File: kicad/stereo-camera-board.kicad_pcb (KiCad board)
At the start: 4 copper layers, 57 x 70 mm, 82 parts, among them IC1 ZLDO1117G33TA, IC2 MCP1700T-2502E/TT, IC3 SN74LVC1T45DCKR, IC4 SN74LVC1T45DCKR, IC5 SN74LVC1T45DCKR, T1 2n2222a, T2 2N2907A, U1 GSB311231HR, U2 ATXMEGA256A3-AU, U3 MAX3207E

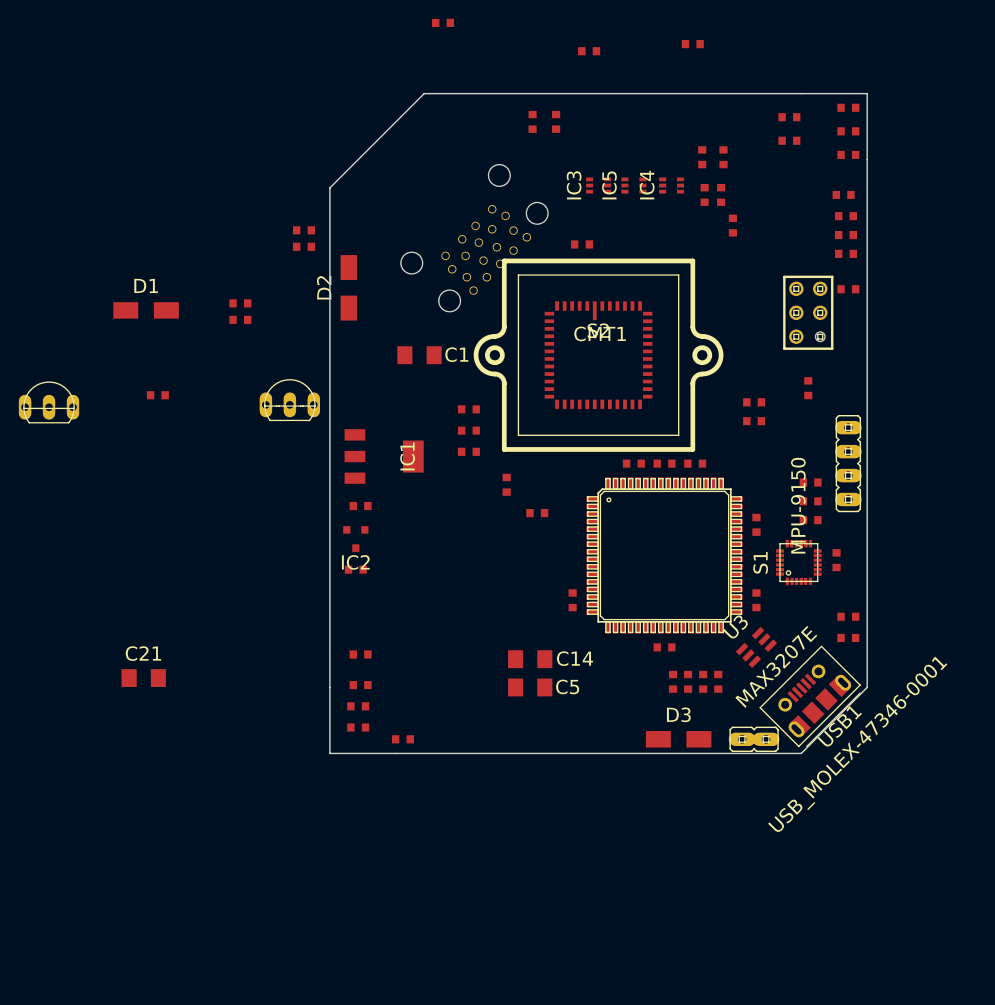
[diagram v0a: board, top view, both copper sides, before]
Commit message: Added mpu-9250 mod file Modified pcb layout
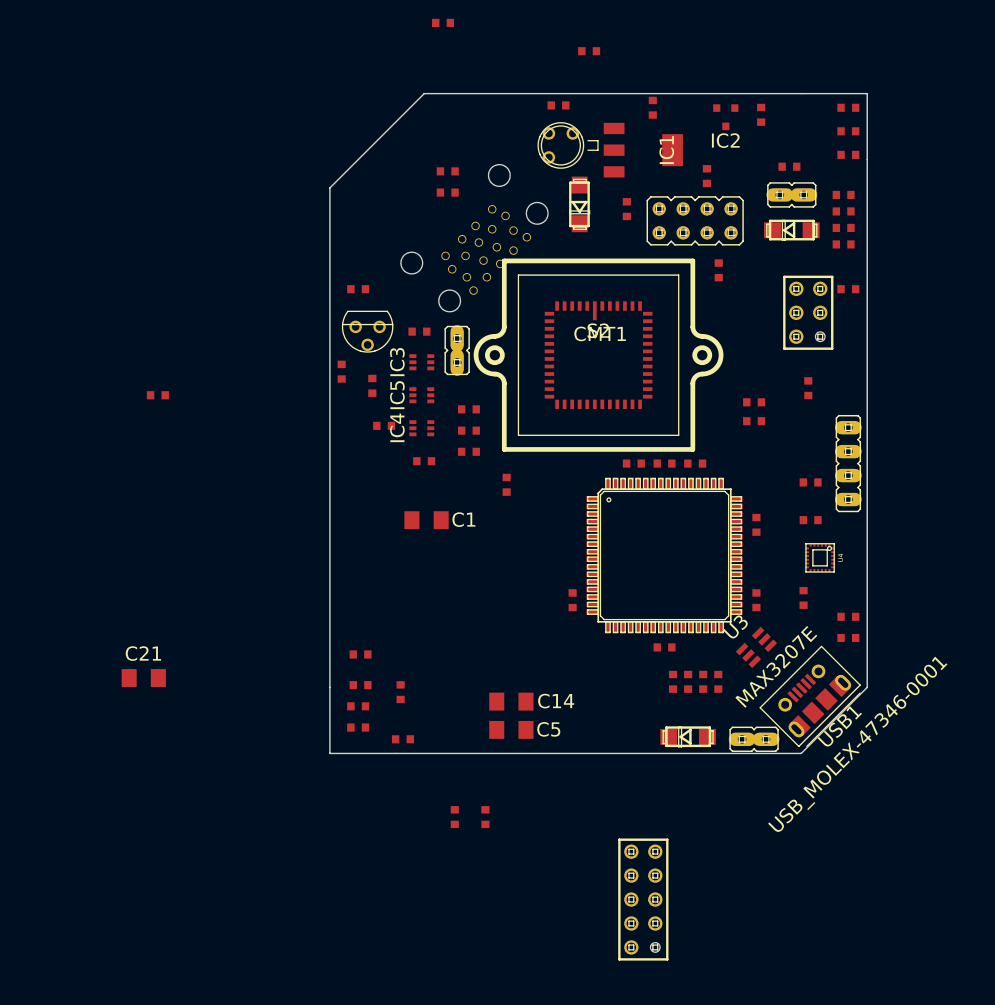
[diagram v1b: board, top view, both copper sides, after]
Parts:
- removed C29: 10nf, SMD-0603
- removed S1: MPU-9150, mpu-9150
- added J1: ~, jumper-JP1, F.Cu at (169.0, 90.8)
- added JP1: ~, jumper-JP4Q, F.Cu at (158.8, 93.5)
- added JP2: JP_JP1Q, jumper-JP1, F.Cu at (133.5, 107.2)
- added JP3: AVR-JTAG-10, atmel-AVR-JTAG-10, F.Cu at (153.2, 165.5)
- added U4: MPU-9250, MPU-9250, F.Cu at (172.0, 129.2)
- C26: value 2.2nf -> .1uf
- C27: value .1uf -> 10nf
- D1, D2, D3: footprint do-214ac -> diode-DO214AC
- T1: footprint transistor-TO92-EBC -> transistor-TO92
- T2: footprint transistor-TO92-EBC -> transistor-TO18
- moved R21 75.6 mm to (133.2, 156.8)
- moved R22 73.7 mm to (136.5, 156.8)
- moved D1 69.0 mm to (169.0, 94.5)
- moved C24 61.8 mm to (127.5, 143.5)
- moved IC2 59.5 mm to (162.0, 82.5)
- moved C7 59.4 mm to (165.8, 82.2), turned to 270 degrees
- moved C6 58.3 mm to (154.2, 81.5), turned to 270 degrees
- moved IC1 42.6 mm to (153.2, 86.0)
- moved C22 42.3 mm to (130.0, 119.0), turned to 180 degrees
- moved T2 38.9 mm to (144.5, 85.5), turned to 180 degrees
- moved IC4 37.0 mm to (129.8, 115.5)
- moved T1 34.6 mm to (124.0, 104.8), turned to 180 degrees
- moved IC5 31.6 mm to (129.8, 112.0)
- moved R20 30.9 mm to (144.2, 81.2)
- moved IC3 26.5 mm to (129.8, 108.5)
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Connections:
- C10 pad 2: N-0000025 (its old number) -> N-00000115
- C12 pad 2: N-0000025 (its old number) -> N-00000115
- C16 pad 1: N-0000013 (its old number) -> N-00000106
- C17 pad 1: N-0000013 (its old number) -> N-00000106
- C18 pad 1: N-0000013 (its old number) -> N-00000106
- C19 pad 1: N-0000013 (its old number) -> N-00000106
- C2 pad 2: N-0000025 (its old number) -> N-00000115
- C20 pad 1: N-0000013 (its old number) -> N-00000106
- C23 pad 1: N-00000143 -> N-00000107
- C26 pad 1: N-0000060 (its old number) -> N-0000037
- C26 pad 2: N-00000101 (its old number) -> N-0000038
- C27 pad 1: N-0000071 -> N-0000037
- C27 pad 2: N-00000101 (its old number) -> N-0000038
- C28 pad 1: N-00000101 (its old number) -> N-00000143
- C3 pad 2: N-0000025 (its old number) -> N-00000115
- C4 pad 2: N-0000025 (its old number) -> N-00000115
- C8 pad 1: N-0000026 -> N-0000028
- C8 pad 2: N-0000023 -> N-000003
- C9 pad 2: N-0000025 (its old number) -> N-00000115
- EXT_SENSOR1 pad 1: N-0000071 -> N-00000114
- EXT_SENSOR1 pad 2: N-00000101 (its old number) -> N-00000108
- FB2 pad 1: N-00000143 -> N-00000106
- FB2 pad 2: N-0000013 (its old number) -> N-00000107
- IC1 pad 3: N-0000039 -> N-0000081
- IC3 pad 5: N-0000034 (its old number) -> N-0000050
- IC4 pad 3: N-0000016 -> N-00000122
- IC4 pad 5: N-0000029 (its old number) -> N-0000042
- IC5 pad 3: N-0000037 -> N-0000051
- IC5 pad 5: N-0000030 (its old number) -> N-0000041
- JP6 pad 2: N-00000122 -> N-00000132
- R10 pad 1: N-0000035 (its old number) -> N-0000073
- R10 pad 2: N-0000088 (its old number) -> N-0000053
- R15 pad 1: N-0000031 -> N-0000052
- R17 pad 1: N-0000041 -> N-0000072
- R17 pad 2: N-0000035 (its old number) -> N-0000073
- R18 pad 1: N-0000040 -> N-0000071
- R18 pad 2: N-00000147 -> N-00000139
- R19 pad 2: N-00000127 (its old number) -> N-00000138
- R20 pad 1: N-0000039 -> N-0000081
- R20 pad 2: N-00000147 -> N-00000139
- R21 pad 1: N-00000146 -> N-00000138
- R23 pad 2: N-0000036 (its old number) -> N-0000080
- R5 pad 1: N-0000025 (its old number) -> N-00000115
- R5 pad 2: N-0000058 (its old number) -> N-0000067
- R7 pad 1: N-00000127 (its old number) -> N-0000061
- S2 pad 12: N-0000025 (its old number) -> N-00000115
- S2 pad 13: N-0000025 (its old number) -> N-00000115
- S2 pad 16: N-00000111 -> N-0000066
- S2 pad 17: N-00000112 -> N-0000065
- S2 pad 18: N-00000113 (its old number) -> N-000008
- S2 pad 19: N-00000114 -> N-0000032
- S2 pad 20: N-000002 (its old number) -> N-0000033
- S2 pad 21: N-00000109 (its old number) -> N-0000023
- S2 pad 22: N-0000064 (its old number) -> N-0000011
- S2 pad 23: N-0000099 (its old number) -> N-0000016
- S2 pad 26: N-00000105 (its old number) -> N-00000118
- S2 pad 27: N-0000027 (its old number) -> N-00000120
- S2 pad 28: N-000003 -> N-00000119
- S2 pad 29: N-0000025 (its old number) -> N-00000115
- S2 pad 30: N-0000011 -> N-00000115
- S2 pad 31: N-000006 (its old number) -> N-00000115
- S2 pad 32: N-0000058 (its old number) -> N-0000067
- S2 pad 33: N-0000063 (its old number) -> N-00000117
- S2 pad 34: N-0000025 (its old number) -> N-00000115
- S2 pad 38: N-0000025 (its old number) -> N-00000115
- S2 pad 41: N-00000115 -> N-00000111
- S2 pad 42: N-0000098 (its old number) -> N-00000112
- S2 pad 43: N-0000078 (its old number) -> N-000005
- S2 pad 44: N-0000079 (its old number) -> N-000009
- S2 pad 45: N-0000080 -> N-00000121
- S2 pad 46: N-00000107 -> N-00000123
- S2 pad 48: N-0000025 (its old number) -> N-00000115
- S2 pad 7: N-0000025 (its old number) -> N-00000115
- U1 pad 10: N-0000054 -> N-00000100
- U1 pad 12: N-00000127 (its old number) -> N-00000138
- U1 pad 3: N-00000127 (its old number) -> N-0000061
- U2 pad 1: N-0000098 (its old number) -> N-00000138
- U2 pad 12: N-00000127 (its old number) -> N-0000054
- U2 pad 15: N-0000013 (its old number) -> N-00000106
- U2 pad 18: N-0000063 (its old number) -> N-0000016
- U2 pad 19: N-0000058 (its old number) -> N-0000011
- U2 pad 2: N-00000115 -> N-0000053
- U2 pad 20: N-000003 -> N-0000023
- U2 pad 21: N-0000027 (its old number) -> N-0000033
- U2 pad 22: N-00000105 (its old number) -> N-0000032
- U2 pad 23: N-0000047 -> N-000008
- U2 pad 25: N-0000013 (its old number) -> N-00000106
- U2 pad 26: N-0000099 (its old number) -> N-0000065
- U2 pad 27: N-0000064 (its old number) -> N-0000066
- U2 pad 28: N-000002 (its old number) -> N-00000110
- U2 pad 3: N-00000114 -> N-00000140
- U2 pad 35: N-0000013 (its old number) -> N-00000106
- U2 pad 36: N-0000014 (its old number) -> N-00000122
- U2 pad 37: N-00000100 -> N-0000080
- U2 pad 39: N-0000088 (its old number) -> N-00000128
- U2 pad 4: N-00000113 (its old number) -> N-00000141
- U2 pad 40: N-0000011 -> N-0000039
- U2 pad 41: N-0000036 (its old number) -> N-0000040
- U2 pad 42: N-0000037 -> N-00000125
- U2 pad 43: N-0000016 -> N-00000124
- U2 pad 45: N-0000013 (its old number) -> N-00000106
- U2 pad 46: N-00000121 -> N-0000067
- U2 pad 47: N-0000051 -> N-00000117
- U2 pad 48: N-0000052 -> N-00000111
- U2 pad 49: N-0000053 -> N-00000112
- U2 pad 5: N-00000112 -> N-00000142
- U2 pad 50: N-000006 (its old number) -> N-000005
- U2 pad 51: N-0000034 (its old number) -> N-000009
- U2 pad 53: N-0000013 (its old number) -> N-00000106
- U2 pad 54: N-0000029 (its old number) -> N-00000121
- U2 pad 55: N-0000030 (its old number) -> N-00000123
- U2 pad 6: N-00000111 -> N-0000051
- U2 pad 61: N-00000143 -> N-00000107
- U2 pad 62: N-0000080 -> N-00000119
- U2 pad 63: N-0000079 (its old number) -> N-00000120
- U2 pad 64: N-0000078 (its old number) -> N-00000118
- U2 pad 7: N-00000110 -> N-0000041
- U2 pad 8: N-00000107 -> N-0000042
- U2 pad 9: N-00000109 (its old number) -> N-0000050
- USB1 pad 1: N-0000031 -> N-0000052

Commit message: Rotated xmega 45d Repositioned some other small components on pcb Cut bottom right corner to match top left
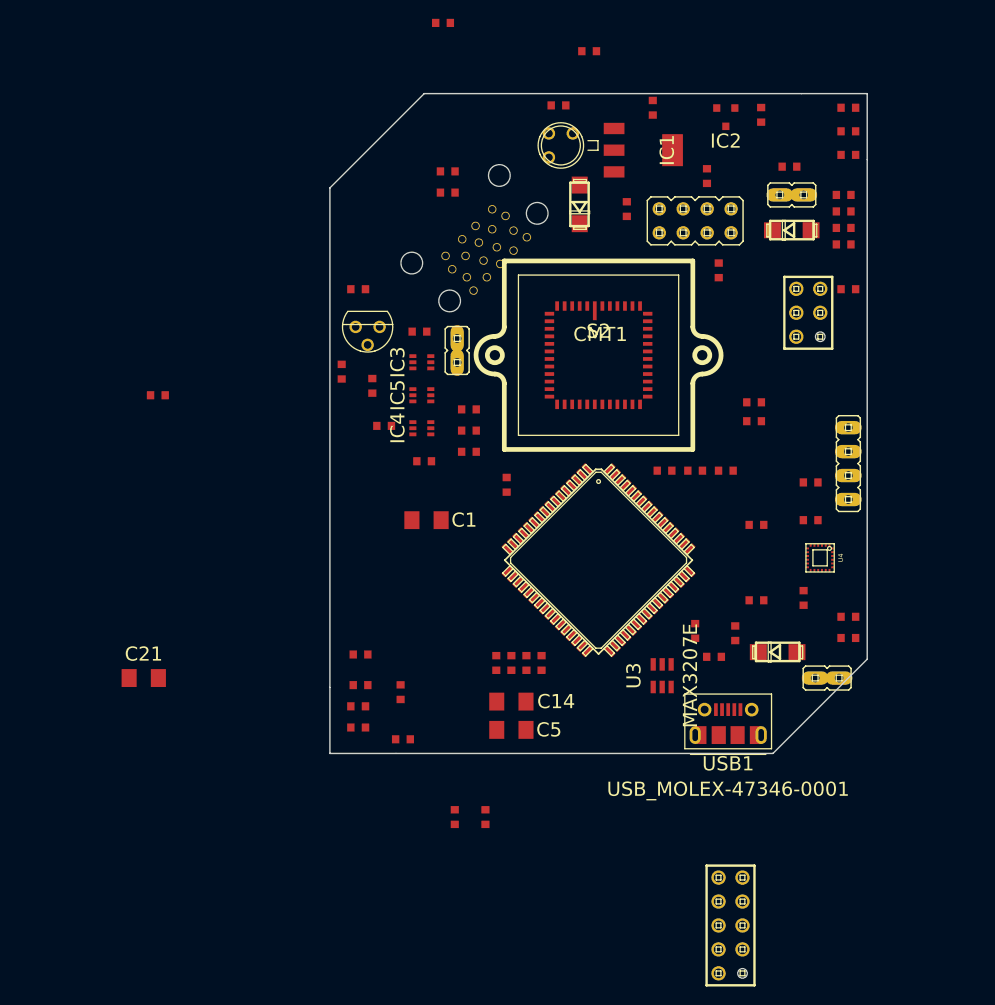
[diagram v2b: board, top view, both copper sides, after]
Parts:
- moved R23 27.1 mm to (163.0, 137.2)
- moved R11 18.9 mm to (139.2, 140.4)
- moved R12 18.9 mm to (137.7, 140.4)
- moved R14 18.9 mm to (140.8, 140.4)
- moved R15 18.9 mm to (142.4, 140.4)
- moved C16 16.2 mm to (160.8, 139.8), turned to 180 degrees
- moved D3 13.1 mm to (167.5, 139.2)
- moved USB1 11.3 mm to (162.2, 149.5), turned to 0 degrees
- moved U3 10.4 mm to (155.2, 141.8), turned to 90 degrees
- moved JP6 10.1 mm to (172.8, 142.0)
- moved JP3 9.65 mm to (162.5, 168.2)
- moved U2 7.02 mm to (148.5, 129.5), turned to 315 degrees
- moved C17 3.69 mm to (158.8, 137.0), turned to 270 degrees
- moved C20 3.34 mm to (162.0, 120.0)
- moved C23 3.34 mm to (155.5, 120.0)
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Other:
- outline, holes or cut-outs redrawn

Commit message: Routed differential signals Routed 9-axis sensor Routed a few small components Set up routing rules for OshPark Fixed netlist Rearranged some nets for better fit
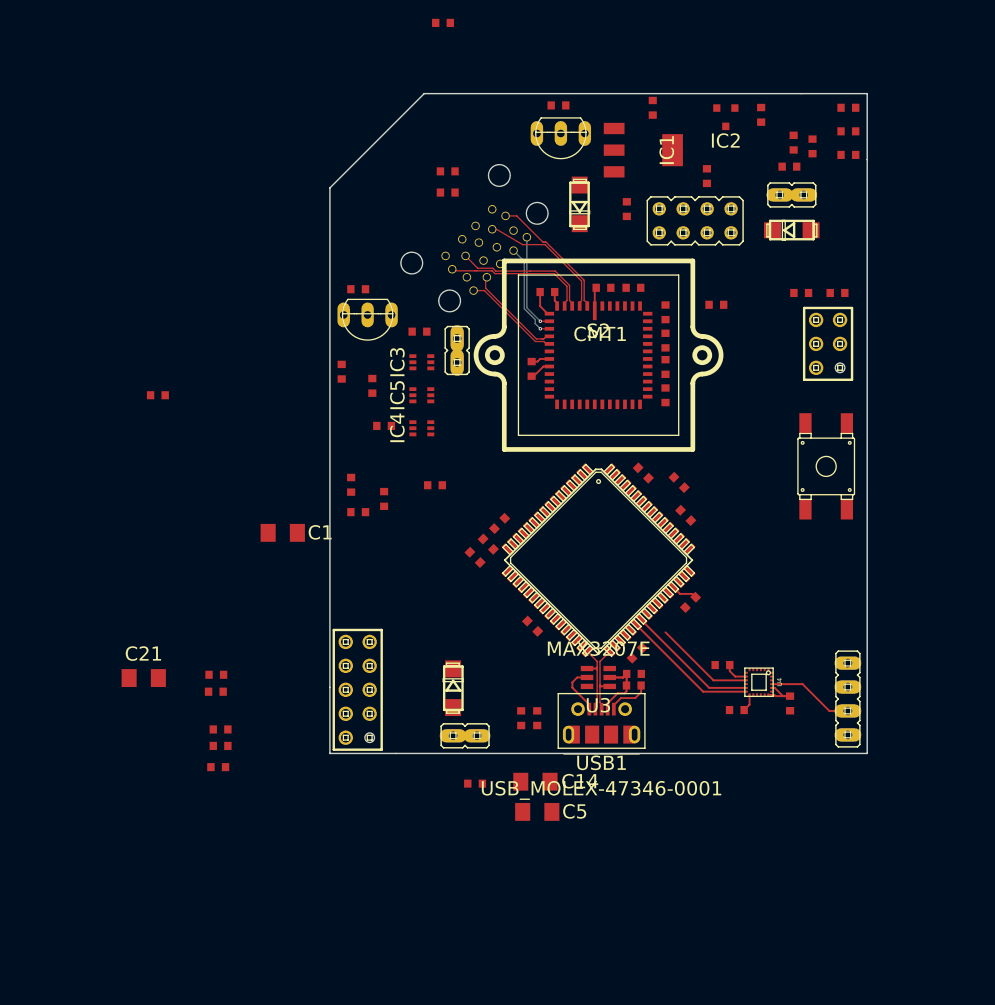
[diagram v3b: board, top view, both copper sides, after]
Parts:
- added P1: FSM4JSMA-SMD, switch-misc-FSM4JSMA-SMD, F.Cu at (172.7, 119.5)
- T1: footprint transistor-TO92 -> transistor-TO92-EBC
- T2: footprint transistor-TO18 -> transistor-TO92-EBC
- moved R12 63.6 mm to (169.2, 85.2)
- moved R11 63.4 mm to (171.2, 85.6)
- moved JP3 46.8 mm to (123.0, 143.2)
- moved JP6 38.9 mm to (134.3, 148.1)
- moved R23 38.2 mm to (152.2, 100.6), turned to 0 degrees
- moved R21 36.9 mm to (122.2, 121.5)
- moved R22 35.4 mm to (125.8, 123.0)
- moved D3 34.6 mm to (133.1, 143.1), turned to 270 degrees
- moved C11 34.1 mm to (170.0, 101.2)
- moved R3 33.9 mm to (135.4, 129.2), turned to 315 degrees
- moved C22 31.6 mm to (108.0, 141.7), turned to 0 degrees
- moved R4 31.1 mm to (136.8, 127.8), turned to 315 degrees
- moved C12 26.3 mm to (155.6, 109.0), turned to 270 degrees
- moved C26 25.4 mm to (163.2, 145.4), turned to 180 degrees
- moved EXT_SENSOR1 25.0 mm to (174.9, 144.2)
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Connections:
- D2 pad A: N-00000126 (its old number) -> N-00000132
- IC1 pad 3: N-0000081 -> N-0000080
- JP1 pad 2: N-000006 (its old number) -> N-0000020
- JP1 pad 4: N-0000012 (its old number) -> N-000003
- JP1 pad 6: N-000002 (its old number) -> N-0000055
- JP1 pad 8: N-0000029 (its old number) -> N-0000056
- JP6 pad 1: N-0000031 (its old number) -> N-0000038
- R10 pad 1: N-0000073 -> N-0000083
- R15 pad 1: N-0000052 -> N-0000038
- R17 pad 1: N-0000072 (its old number) -> N-0000082
- R17 pad 2: N-0000073 -> N-0000083
- R18 pad 1: N-0000071 (its old number) -> N-0000081
- R18 pad 2: N-00000139 (its old number) -> N-00000143
- R20 pad 1: N-0000081 -> N-0000080
- R20 pad 2: N-00000139 (its old number) -> N-00000143
- S2 pad 10: N-0000012 (its old number) -> N-0000055
- S2 pad 11: N-000006 (its old number) -> N-0000056
- S2 pad 8: N-000002 (its old number) -> N-000003
- S2 pad 9: N-0000029 (its old number) -> N-0000020
- U1 pad 14: N-0000012 (its old number) -> N-000003
- U1 pad 15: N-000006 (its old number) -> N-0000020
- U1 pad 17: N-000002 (its old number) -> N-0000055
- U1 pad 18: N-0000029 (its old number) -> N-0000056
- U2 pad 32: N-0000078 (its old number) -> N-0000073
- U2 pad 33: N-0000077 (its old number) -> N-0000074
- U3 pad 1: N-0000078 (its old number) -> N-0000074
- U3 pad 4: N-0000077 (its old number) -> N-0000073
- U3 pad 5: N-0000031 (its old number) -> N-0000038
- USB1 pad 1: N-0000052 -> N-0000038
- USB1 pad 2: N-0000078 (its old number) -> N-0000073
- USB1 pad 3: N-0000077 (its old number) -> N-0000074
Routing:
- net N-00000115: track 0.00 -> 14.6 mm
- net N-00000130: track 0.00 -> 14.6 mm
- net N-0000069: track 0.00 -> 14.2 mm
- net N-00000129: track 0.00 -> 14.1 mm
- net N-0000072: track 0.00 -> 13.8 mm
- net N-0000064: track 0.00 -> 13.6 mm
- net N-0000037: track 0.00 -> 10.7 mm
- net N-000003: track 0.00 -> 10.0 mm, vias 0 -> 1
- net N-0000020: track 0.00 -> 10.0 mm, vias 0 -> 1
- net N-0000056: track 0.00 -> 9.95 mm
- net N-0000055: track 0.00 -> 9.91 mm
- net N-00000111: track 0.00 -> 9.26 mm
- net N-0000073: track 0.00 -> 8.87 mm
- net N-0000074: track 0.00 -> 8.78 mm
- net N-0000077: track 0.00 -> 6.96 mm
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- added copper zone on Inner1.Cu, net (none)
- added copper zone on Inner2.Cu, net (none)
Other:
- outline, holes or cut-outs redrawn
- net class Default: clearance 0.254 -> 0.1; trace_width 0.254 -> 0.2032
- net class USB added: clearance 0.1, trace_width 0.127, via_dia 0.3556, via_drill 0.254
- rule trace_clearance: 0.254 -> 0.1
- rule trace_min: 0.254 -> 0.127
- rule via_min_drill: 0.508 -> 0.254
- rule via_min_size: 0.889 -> 0.1016

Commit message: Minor component placement adjustments
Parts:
- moved C27 1.32 mm to (163.0, 140.7), turned to 90 degrees
- moved C26 0.79 mm to (163.7, 144.8)
- moved C6 0.19 mm to (154.4, 81.6), turned to 0 degrees
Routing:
- net N-00000143: track 0.00 -> 32.1 mm
- net N-0000091: track 0.00 -> 27.5 mm
- net N-0000036: track 0.00 -> 25.8 mm, vias 0 -> 2
- net N-0000047: track 0.00 -> 20.0 mm, vias 0 -> 2
- net N-00000123: track 0.00 -> 18.9 mm, vias 0 -> 2
- net N-00000131: track 0.00 -> 16.8 mm, vias 0 -> 2
- net N-00000112: track 0.00 -> 13.1 mm
- net N-0000045: track 0.00 -> 8.98 mm
- net N-000004: track 0.00 -> 8.17 mm
- net N-00000109: track 2.74 -> 10.8 mm
- net N-00000124: track 0.00 -> 7.60 mm
- net N-00000125: track 0.00 -> 6.97 mm
- net N-0000038: track 5.36 -> 12.3 mm
- net N-0000027: track 0.00 -> 3.26 mm
- net N-0000070: track 0.00 -> 2.80 mm
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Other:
- net class Default: via_dia 0.889 -> 0.635; via_drill 0.635 -> 0.381
